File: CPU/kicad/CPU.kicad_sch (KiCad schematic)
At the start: 13 parts, among them IC1 71256SA20TPGI, J1 Conn_02x20_Odd_Even, U1 W65C02SxP, U2 74HC00

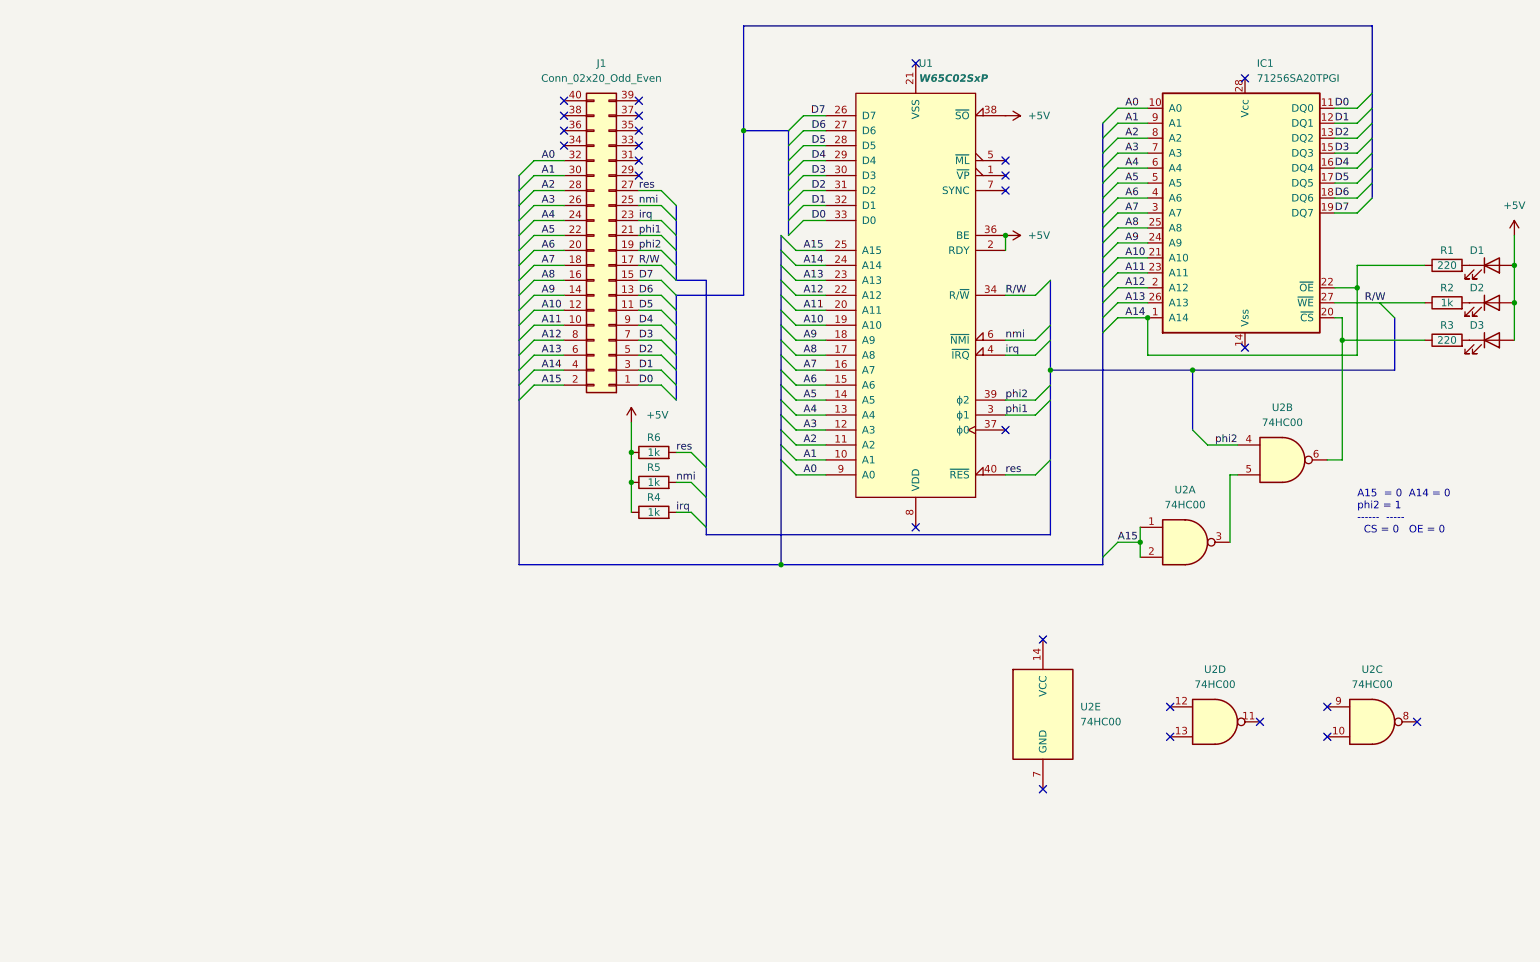
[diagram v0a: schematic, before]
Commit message: add oscillator, extend memory map
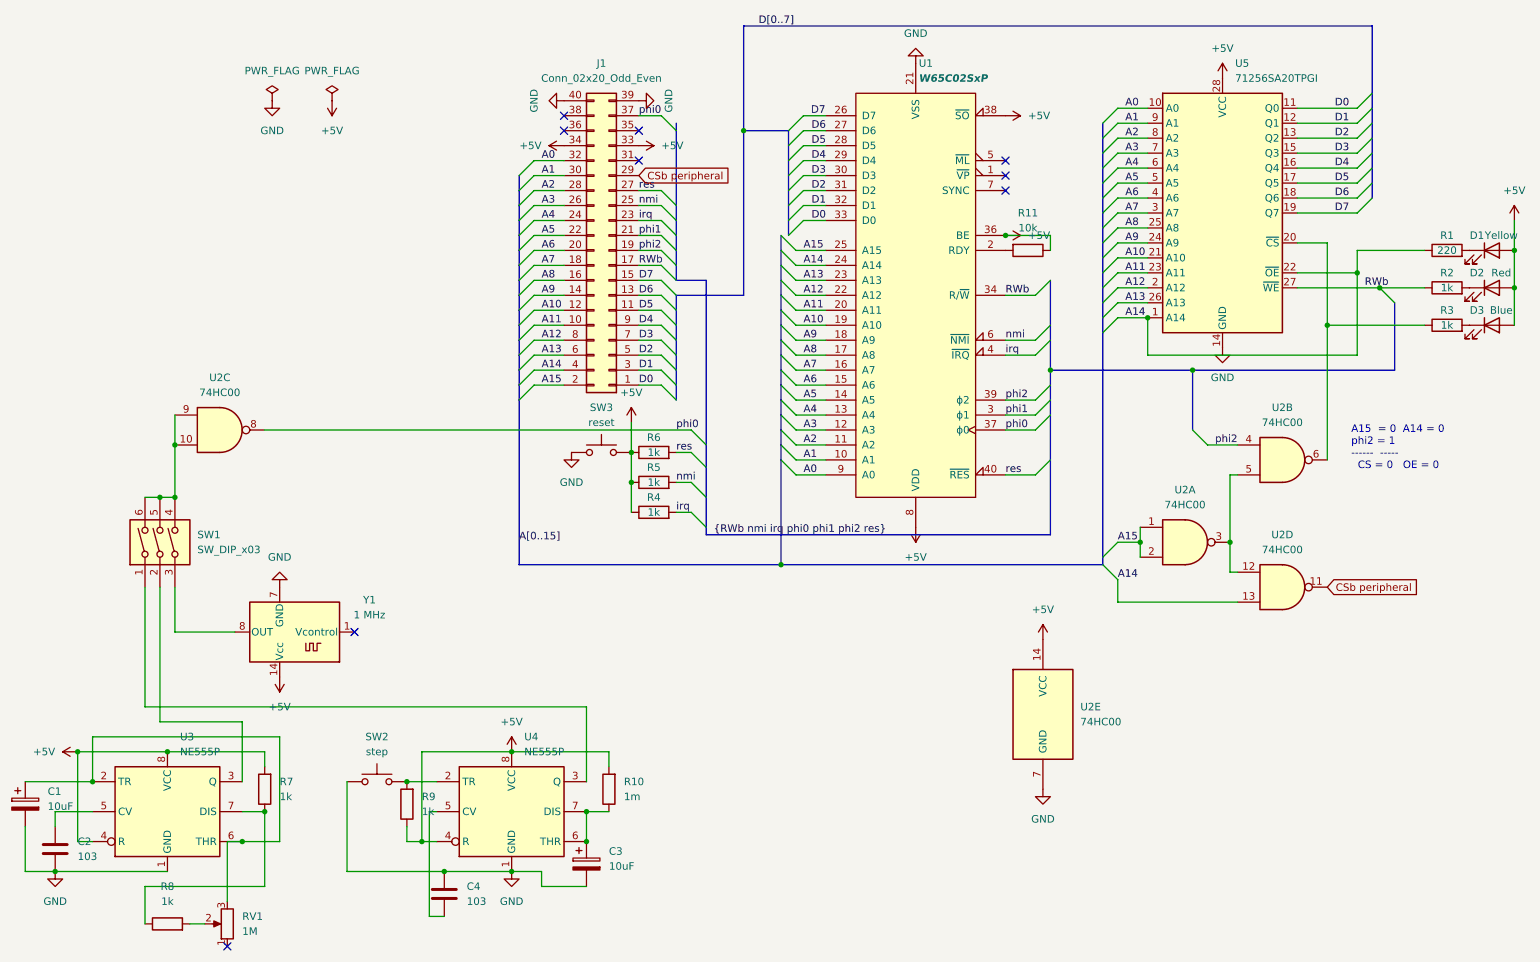
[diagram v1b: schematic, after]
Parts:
- removed IC1: 71256SA20TPGI, Package_DIP:DIP-28_W7.62mm_LongPads, symbol IDT:71256SA20TPGI
- added C1, C3: 10uF, Capacitor_THT:CP_Axial_L10.0mm_D4.5mm_P15.00mm_Horizontal, symbol Device:C_Polarized
- added C2, C4: 103, Capacitor_THT:CP_Axial_L10.0mm_D4.5mm_P15.00mm_Horizontal, symbol Device:C
- added R10: 1m, Resistor_THT:R_Axial_DIN0204_L3.6mm_D1.6mm_P5.08mm_Horizontal, symbol Device:R
- added R11: 10k, Resistor_THT:R_Axial_DIN0204_L3.6mm_D1.6mm_P5.08mm_Horizontal, symbol Device:R
- added R7, R8, R9: 1k, Resistor_THT:R_Axial_DIN0204_L3.6mm_D1.6mm_P5.08mm_Horizontal, symbol Device:R
- added RV1: 1M, Potentiometer_THT:Potentiometer_ACP_CA6-H2,5_Horizontal, symbol Device:R_Potentiometer
- added SW1: SW_DIP_x03, Button_Switch_THT:SW_DIP_SPSTx01_Piano_10.8x4.1mm_W7.62mm_P2.54mm, symbol Switch:SW_DIP_x03
- added SW2: step, Button_Switch_THT:KSA_Tactile_SPST, symbol Switch:SW_Push
- added SW3: reset, Button_Switch_THT:KSA_Tactile_SPST, symbol Switch:SW_Push
- added U3, U4: NE555P, Package_DIP:DIP-8_W7.62mm, symbol Timer:NE555P
- added U5: 71256SA20TPGI, Package_DIP:DIP-28_W15.24mm, symbol Memory_RAM:HM62256BLP
- added Y1: 1 MHz, Oscillator:Oscillator_DIP-14, symbol Oscillator:OCXO-14
- D1: value (none) -> Yellow; footprint (none) -> LED_THT:LED_D1.8mm_W1.8mm_H2.4mm_Horizontal_O6.35mm_Z1.6mm
- D2: value (none) -> Red; footprint (none) -> LED_THT:LED_D1.8mm_W1.8mm_H2.4mm_Horizontal_O6.35mm_Z1.6mm
- D3: value (none) -> Blue; footprint (none) -> LED_THT:LED_D1.8mm_W1.8mm_H2.4mm_Horizontal_O6.35mm_Z1.6mm
- R1, R2, R4, R5, R6: footprint (none) -> Resistor_THT:R_Axial_DIN0204_L3.6mm_D1.6mm_P5.08mm_Horizontal
- R3: value 220 -> 1k; footprint (none) -> Resistor_THT:R_Axial_DIN0204_L3.6mm_D1.6mm_P5.08mm_Horizontal
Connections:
- net +5V: now also J1.33 (Pin_33), J1.34 (Pin_34), U1.8 (VDD), U2.14 (VCC), R10.2, R11.1, R7.2, R9.1, SW3.2, U3.4 (R), U3.8 (VCC), U4.4 (R), U4.8 (VCC), U5.28 (VCC), Y1.14 (Vcc); no longer U1.2 (RDY)
- net A0: now also U5.10 (A0)
- net A1: now also U5.9 (A1)
- net A10: now also U5.21 (A10)
- net A11: now also U5.23 (A11)
- net A12: now also U5.2 (A12)
- net A13: now also U5.26 (A13)
- net A14: now also U2.13, U5.1 (A14), U5.22 (~{OE})
- net A2: now also U5.8 (A2)
- net A3: now also U5.7 (A3)
- net A4: now also U5.6 (A4)
- net A5: now also U5.5 (A5)
- net A6: now also U5.4 (A6)
- net A7: now also U5.3 (A7)
- net A8: now also U5.25 (A8)
- net A9: now also U5.24 (A9)
- net D0: now also U5.11 (Q0)
- net D1: now also U5.12 (Q1)
- net D2: now also U5.13 (Q2)
- net D3: now also U5.15 (Q3)
- net D4: now also U5.16 (Q4)
- net D5: now also U5.17 (Q5)
- net D6: now also U5.18 (Q6)
- net D7: now also U5.19 (Q7)
- net GND: now reaches U2.7 (GND)
- net GND: now also J1.39 (Pin_39), J1.40 (Pin_40), U1.21 (VSS), C1.2, C2.2, C3.2, C4.1, SW2.1, SW3.1, U3.1 (GND), U4.1 (GND), U5.14 (GND), Y1.7 (GND)
- net at R3.1, U2.6: now also U5.20 (~{CS})
- net CSb peripheral: now reaches J1.29 (Pin_29)
- net CSb peripheral: now also U2.11
- net phi0: now reaches J1.37 (Pin_37)
- net phi0: now also U1.37 (ϕ0), U2.8
- net at U2.12: now also U2.3, U2.5
- net at U2.10: now also U2.9, SW1.4, SW1.5, SW1.6
- net R/W renamed RWb
- net RWb: now also U5.27 (~{WE})
- new net: C3.1, R10.1, U4.6 (THR), U4.7 (DIS)
- new net: R9.2, SW2.2, U4.2 (TR)
- new net: C2.1, U3.5 (CV)
- new net: R11.2, U1.2 (RDY)
- new net: C1.1, RV1.3, U3.2 (TR), U3.6 (THR)
- new net: SW1.2, U3.3 (Q)
- new net: R7.1, R8.1, U3.7 (DIS)
- new net: SW1.1, U4.3 (Q)
- new net: SW1.3, Y1.8 (OUT)
- new net: C4.2, U4.5 (CV)
- new net: R8.2, RV1.2
- no-connect marks 26 -> 9
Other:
- moved on the sheet: D1, D2, D3, R1, R2, R3, U2C, U2D

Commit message: updates
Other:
- note added: "missing on conn: - res - CSb peripheral"
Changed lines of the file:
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@@
 	(generator_version "9.0")
 	(paper "A4")
+	(text "missing on conn:\n- res\n- CSb peripheral"
+		(exclude_from_sim no)
+		(at 75.184 65.024 0)
+		(effects
+			(font
+				(size 1.27 1.27)
+			)
+		)
+	)
 	(text "A15  = 0  A14 = 0\nphi2 = 1\n------  -----\n  CS = 0   OE = 0"
 		(exclude_from_sim no)
@@
 	(bus
 		(pts
-			(xy 100.33 92.71) (xy 100.33 120.65)
-		)
-		(stroke
-			(width 0)
-			(type default)
-		)
-	)
-	(bus
-		(pts
 			(xy 199.39 78.74) (xy 199.39 81.28)
 		)
@@
 		)
 	)
+	(bus
+		(pts
+			(xy 100.33 92.71) (xy 100.33 120.65)
+		)
+		(stroke
+			(width 0)
+			(type default)
+		)
+	)
 	(wire
 		(pts
@@
 	)
 	(label "A[0..15]"
-		(at 100.33 116.84 0)
+		(at 100.33 119.38 0)
 		(effects
 			(font
